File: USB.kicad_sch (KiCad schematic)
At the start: 15 parts, among them J4 USB_C_Receptacle_USB2.0_16P, U1 USBLC6-2SC6, U6 FT230XS

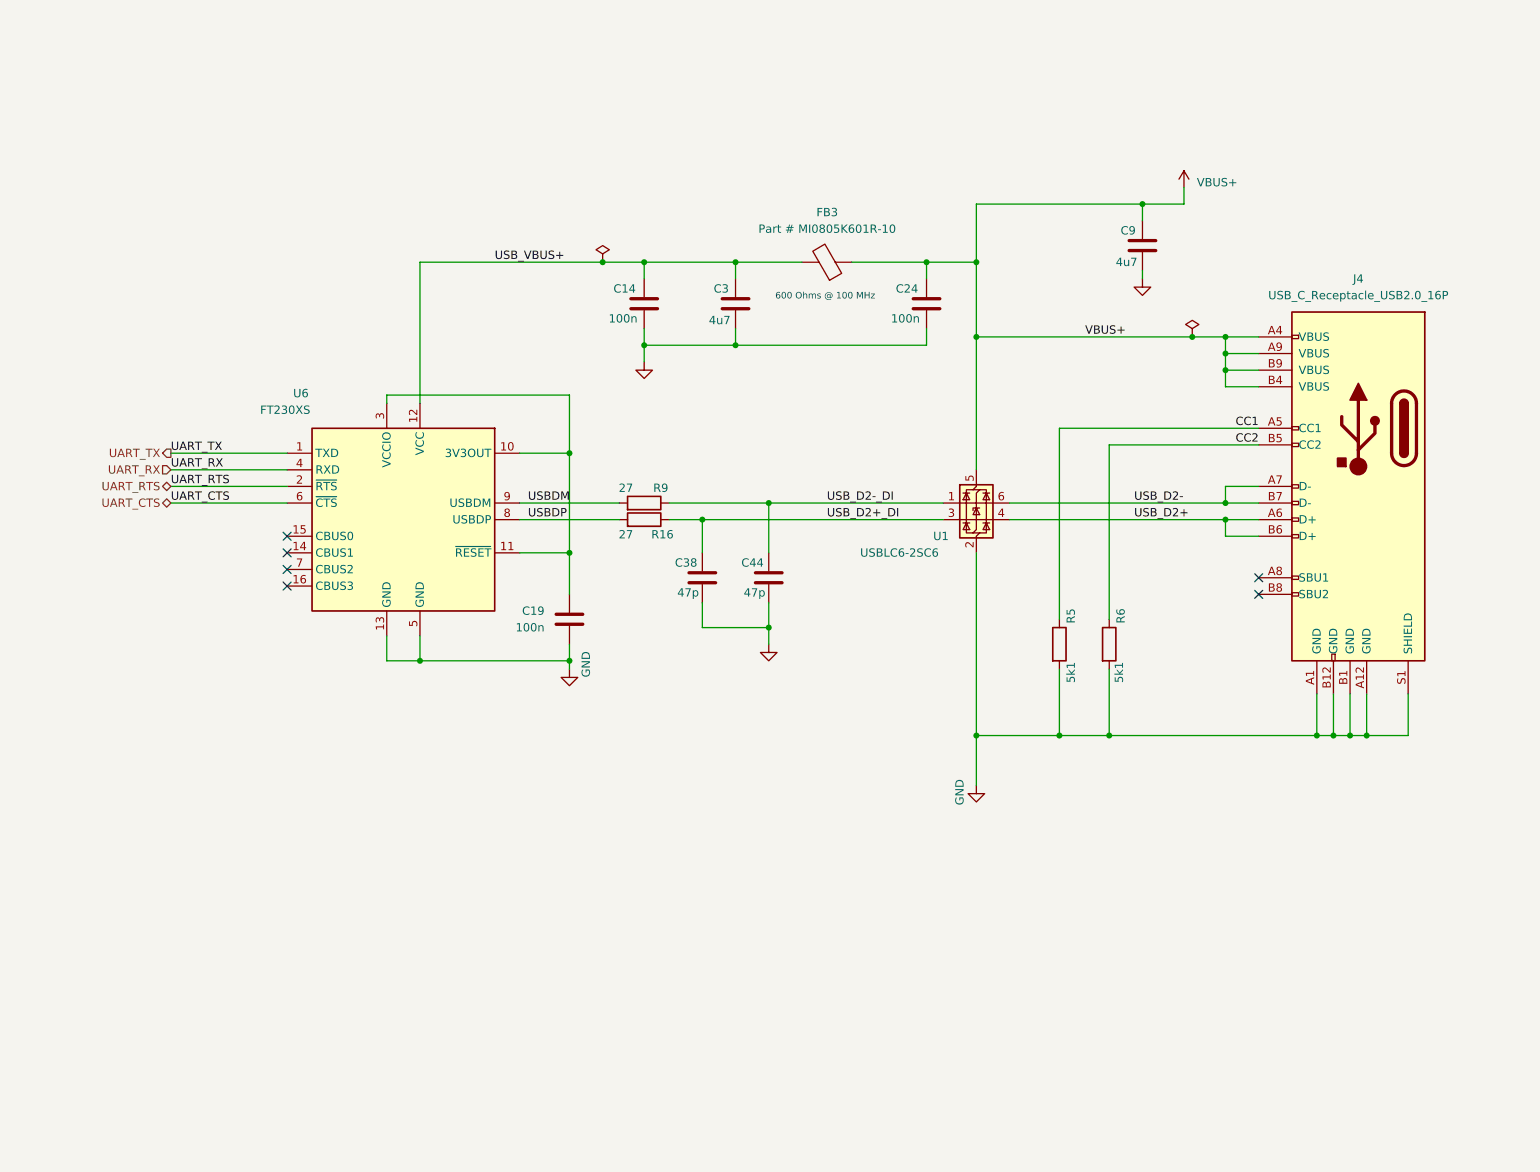
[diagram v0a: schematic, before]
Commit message: Schematics Update
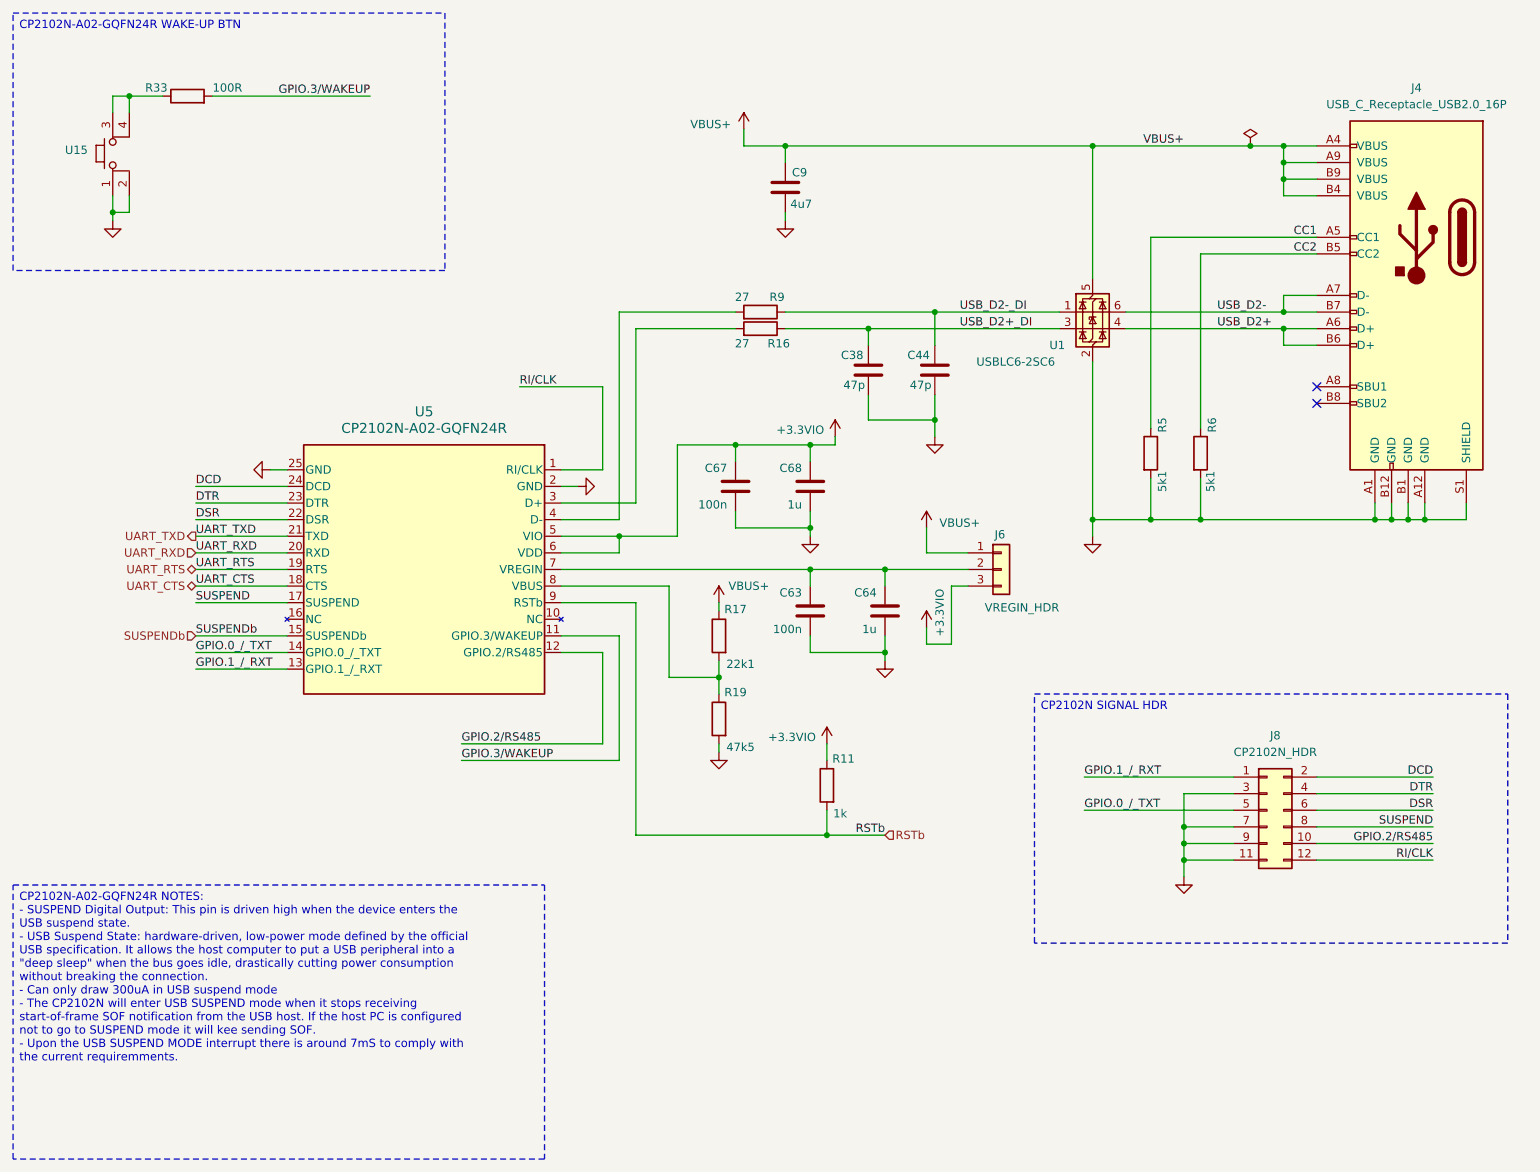
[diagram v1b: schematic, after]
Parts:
- removed C14, C19, C24: 100n, Capacitor_SMD:C_0805_2012Metric, symbol Device:C
- removed C3: 4u7, Capacitor_SMD:C_0805_2012Metric, symbol Device:C
- removed FB3: Part # MI0805K601R-10, Capacitor_SMD:C_0805_2012Metric, symbol Device:FerriteBead
- removed U6: FT230XS, Package_SO:SSOP-16_3.9x4.9mm_P0.635mm, symbol Interface_USB:FT230XS
- added C63, C67: 100n, Capacitor_SMD:C_0805_2012Metric, symbol Device:C
- added C64, C68: 1u, Capacitor_SMD:C_0805_2012Metric, symbol Device:C
- added J6: VREGIN_HDR, symbol Connector_Generic:Conn_01x03
- added J8: CP2102N_HDR, symbol Connector_Generic:Conn_02x06_Odd_Even
- added R11: 1k, Resistor_SMD:R_0805_2012Metric, symbol Device:R
- added R17: 22k1, Resistor_SMD:R_0603_1608Metric, symbol Device:R
- added R19: 47k5, Resistor_SMD:R_0603_1608Metric, symbol Device:R
- added R33: 100R, Resistor_SMD:R_0805_2012Metric, symbol Device:R
- added U15: (no value), Personal_Project:Button_SKSCLCE010, symbol Personal_Projects:BTN_SKSCLCE010
- added U5: CP2102N-A02-GQFN24R, Personal_Projects:CP2102N_A02_GQFN24R_QFN24_SIL, symbol Personal_Components:CP2102N-A02-GQFN24R
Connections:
- net GND: now also C63.2, C64.2, C67.2, C68.2, J8.11 (Pin_11), J8.3 (Pin_3), J8.7 (Pin_7), J8.9 (Pin_9), R19.2, U15.1, U15.2, U5.2 (GND), U5.25 (GND)
- net UART_CTS: now also U5.18 (CTS)
- net UART_RTS: now also U5.19 (RTS)
- net VBUS+: now also J6.1 (Pin_1), R17.1
- net USBDM: no longer names the net of R9.2
- net USBDM: now also U5.4 (D-)
- net USBDP: no longer names the net of R16.2
- net USBDP: now also U5.3 (D+)
- new net: R17.2, R19.1, U5.8 (VBUS)
- new net: R33.1, U15.3, U15.4
- new net: C63.1, C64.1, J6.2 (Pin_2), U5.7 (VREGIN)
- new net +3.3VIO: C67.1, C68.1, J6.3 (Pin_3), R11.1, U5.5 (VIO), U5.6 (VDD)
- new net DCD: J8.2 (Pin_2), U5.24 (DCD)
- new net DSR: J8.6 (Pin_6), U5.22 (DSR)
- new net DTR: J8.4 (Pin_4), U5.23 (DTR)
- new net GPIO.0_/_TXT: J8.5 (Pin_5), U5.14 (GPIO.0_/_TXT)
- new net GPIO.1_/_RXT: J8.1 (Pin_1), U5.13 (GPIO.1_/_RXT)
- new net GPIO.2/RS485: J8.10 (Pin_10), U5.12 (GPIO.2/RS485)
- new net GPIO.3/WAKEUP: R33.2, U5.11 (GPIO.3/WAKEUP)
- new net RI/CLK: J8.12 (Pin_12), U5.1 (RI/CLK)
- new net RSTb: R11.2, U5.9 (RSTb)
- new net SUSPEND: J8.8 (Pin_8), U5.17 (SUSPEND)
- new net SUSPENDb: U5.15 (SUSPENDb)
- new net UART_RXD: U5.20 (RXD)
- new net UART_TXD: U5.21 (TXD)
- no-connect marks 6 -> 2
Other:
- note removed: "600 Ohms @ 100 MHz"
- title: LoRa Board -> LoRa STM32WL55CCU6 Board
- moved on the sheet: C38, C44, C9, J4, R16, R5, R6, R9, U1
